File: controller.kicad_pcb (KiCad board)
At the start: 2 copper layers, 60 x 122 mm, 150 parts, among them J1 KYCON_KPJX-4S-S, J10 MicroFit_2x04, J11 Phoenix MPT, J12 MicroFit_2x04, J13 JST_B2B-XH, J14 Phoenix MPT, J16 MLX_1x03, J17 MLX_1x03, J2 MicroFit_2x02, J3 24V/5A OUT, J4 DB25 FEMALE, J5 Phoenix MPT, J6 Phoenix MPT, J7 MicroFit_2x04, J8 Phoenix MPT, J9 Phoenix MPT, K1 OJS-SH-124HMF, Q1 BC847, Q2 IRF9540SPBF, Q3 BC857, Q4 BC847, Q5 BC857, U1 MC78M12CDT-TR, U2 MAX5035BUSA, U3 LM358, U4 74HC245, U5 74HC245, U6 ACSL-6310, U7 ACSL-6310

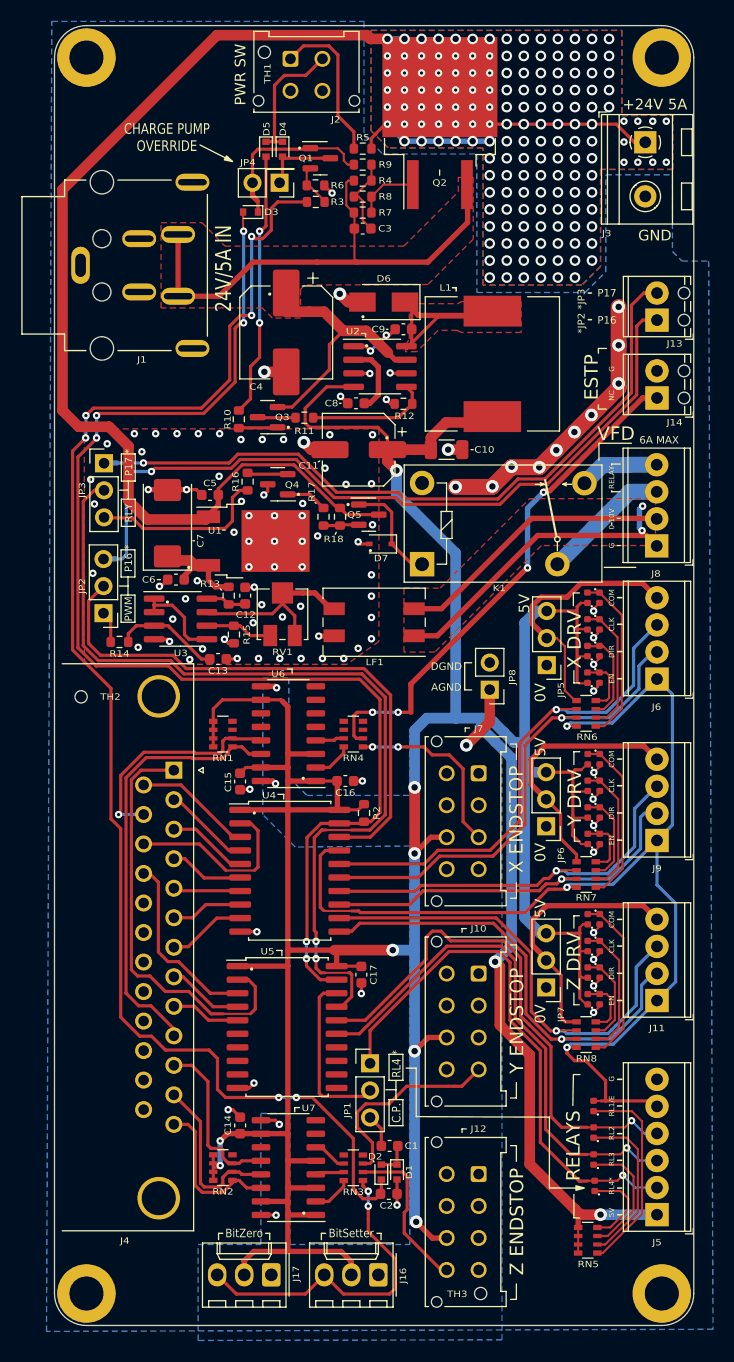
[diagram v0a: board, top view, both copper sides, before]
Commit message: Moved LPT left to protrude just over the PCB edge. Moved power connector inward to increase 24V/GND clearance.
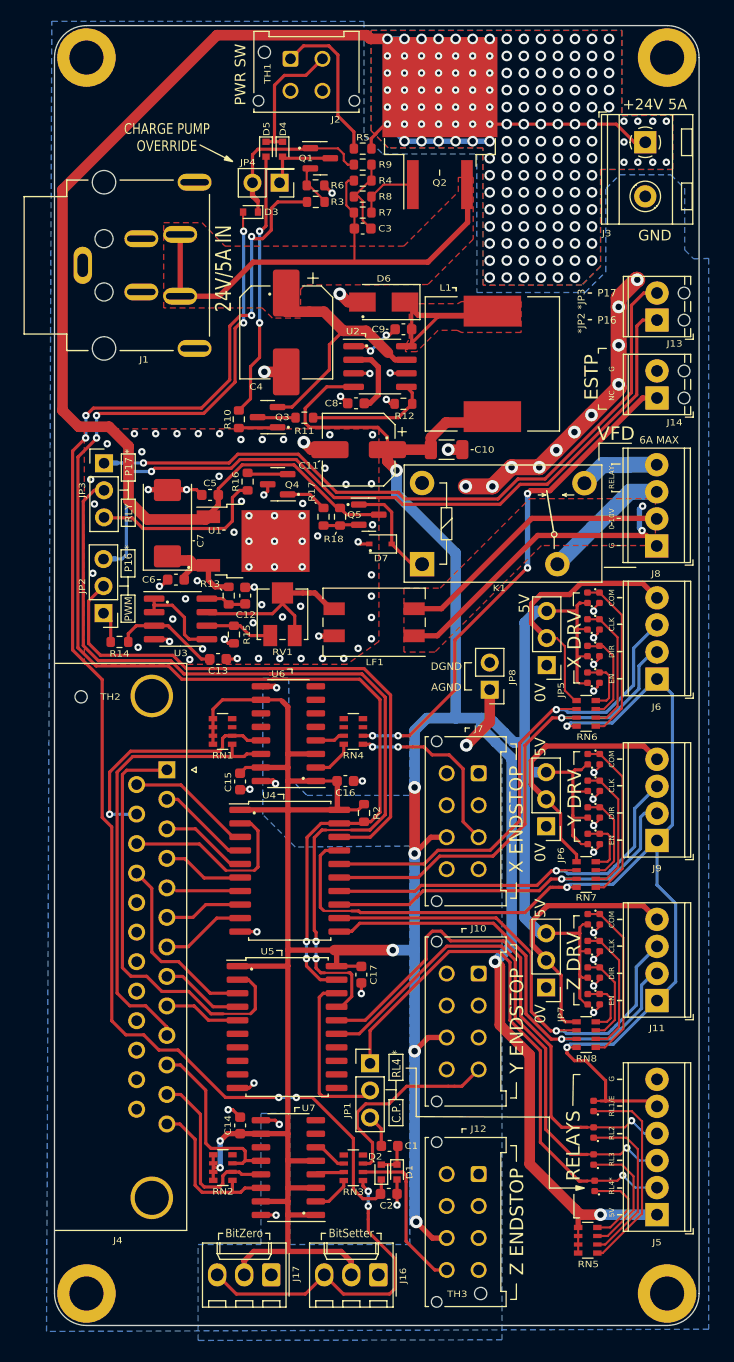
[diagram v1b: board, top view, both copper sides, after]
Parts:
- moved NT13 2.21 mm to (90.8, 112.0)
- moved J4 0.66 mm to (68.3, 115.2)
- moved H2 0.50 mm to (115.2, 48.4)
- moved H4 0.50 mm to (115.2, 164.4)
- moved NT20 0.44 mm to (104.8, 126.3)
- moved RN1 0.25 mm to (73.5, 111.7)
- moved RN4 0.24 mm to (85.8, 111.7)
- moved J1 0.20 mm to (69.5, 67.9)
- moved NT11 0.14 mm to (90.8, 153.6)
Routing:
- net /Connectors/EMERG_STOP_OUT: track 7.73 -> 3.75 mm
- net /Connectors/EMRG_STOP: track 40.2 -> 43.2 mm
- net GND: track 77.3 -> 79.7 mm, vias 101 -> 102
- net /LPT Interface/P10_OUT: track 41.1 -> 42.9 mm
- net /LPT Interface/P15_OUT: track 21.1 -> 22.8 mm
- net /LPT Interface/P11_OUT: track 16.0 -> 17.3 mm
- net /LPT Interface/P1_IN: track 39.8 -> 41.0 mm
- net /LPT Interface/P12_OUT: track 16.2 -> 17.3 mm
- net /LPT Interface/P2_IN: track 7.03 -> 8.10 mm
- net Net-(C2-Pad1): track 134.0 -> 133.0 mm
- net /LPT Interface/P17_IN: track 16.7 -> 17.6 mm
- net /LPT Interface/P8_IN: track 7.14 -> 7.81 mm
- net /LPT Interface/P16_IN: track 17.3 -> 17.9 mm
- net /LPT Interface/P14_IN: track 10.4 -> 11.1 mm
- net /LPT Interface/P9_IN: track 6.51 -> 7.18 mm
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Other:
- board size 60 x 122 mm -> 60.5 x 122 mm

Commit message: JLCPCB_V2.0_FROZEN
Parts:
- moved C10 2.78 mm to (97.3, 85.2), turned to 0 degrees
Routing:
- net GND: track 79.7 -> 85.2 mm, vias 102 -> 105
- net /Power/U2_FB: track 30.8 -> 33.4 mm
- net 24V_SAFE: track 133.9 -> 134.4 mm

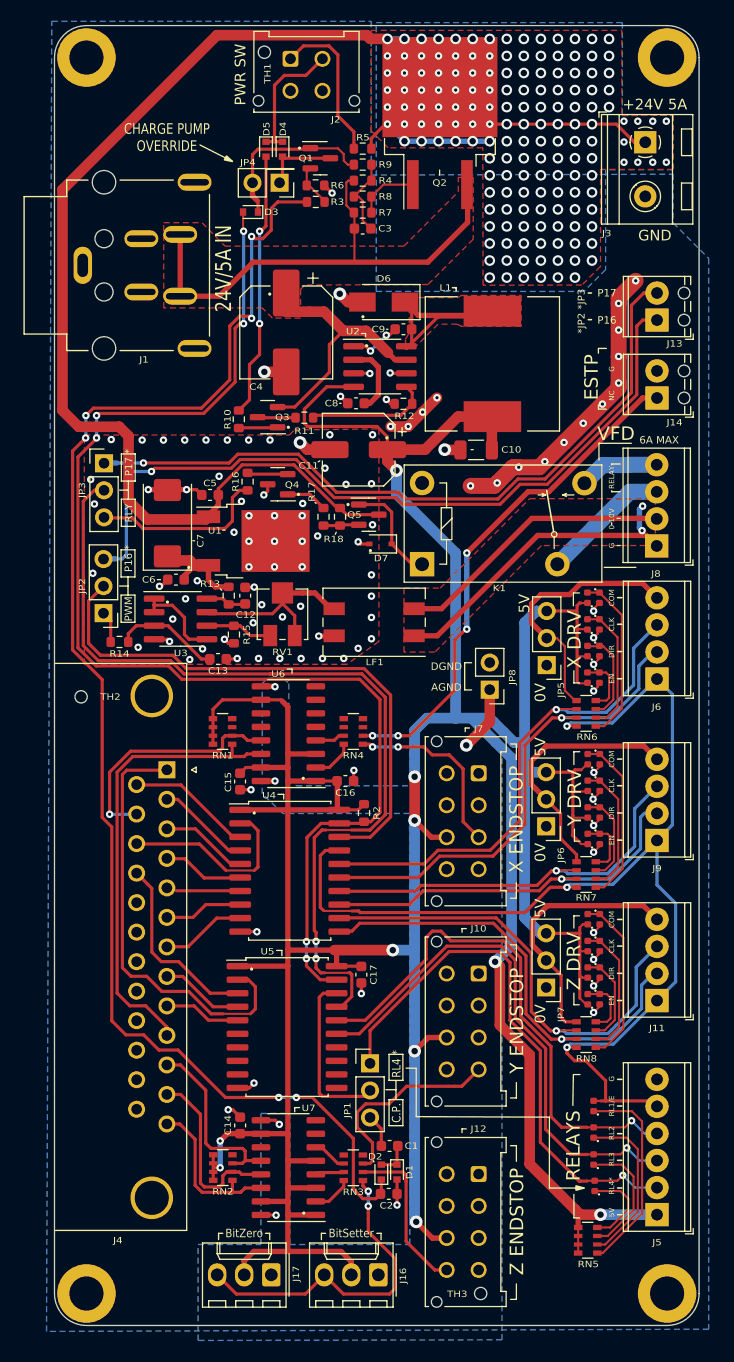
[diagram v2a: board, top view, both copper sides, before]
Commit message: V2.1 after errors found on physical V2.0 boards. sigh
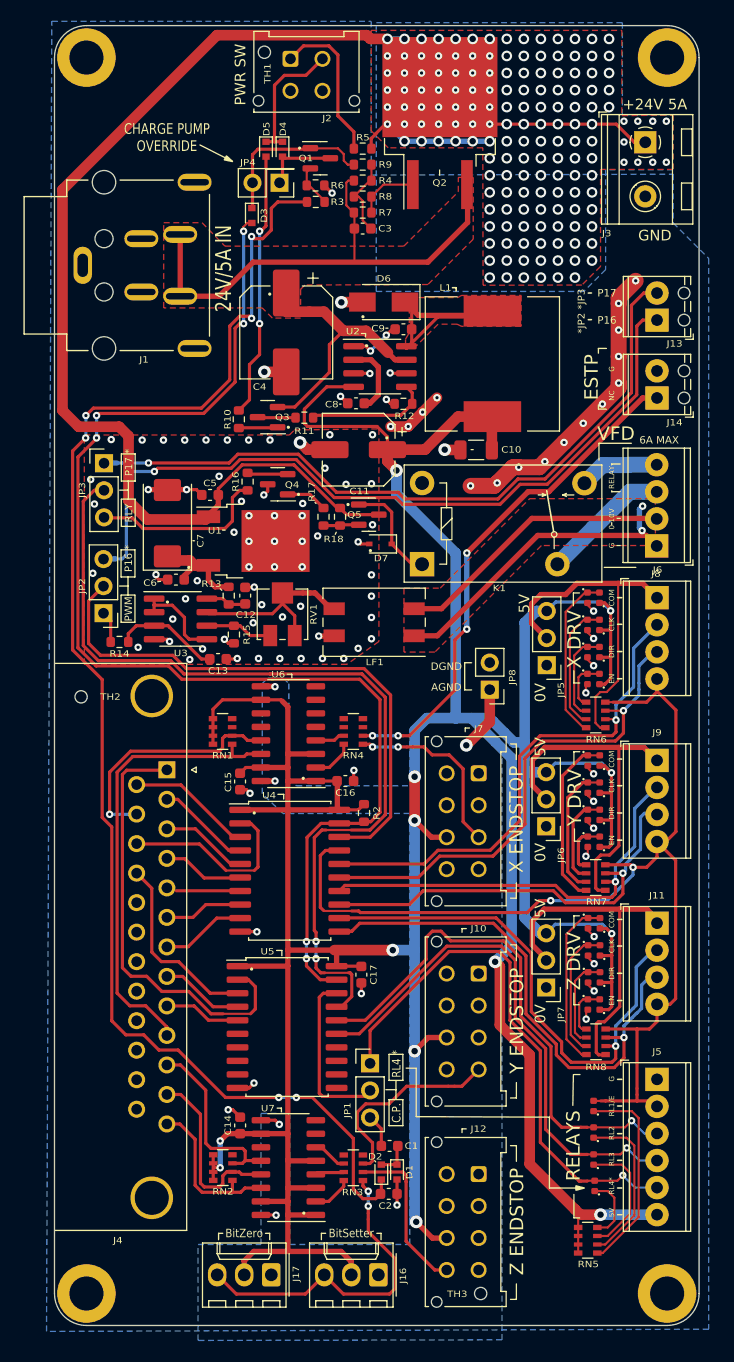
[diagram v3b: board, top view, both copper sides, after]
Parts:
- moved J5 12.7 mm to (114.3, 144.3), turned to -90 degrees
- moved D29 8.08 mm to (108.9, 137.3)
- moved D28 8.08 mm to (107.8, 137.3)
- moved D20 7.83 mm to (107.8, 122.0)
- moved D21 7.83 mm to (108.9, 122.0)
- moved D12 7.71 mm to (107.8, 106.7)
- moved D13 7.71 mm to (108.9, 106.7)
- moved J6 7.63 mm to (114.3, 99.1), turned to -90 degrees
- moved D18 7.58 mm to (107.8, 99.1)
- moved D19 7.58 mm to (108.9, 99.1)
- moved J9 7.51 mm to (114.3, 114.4), turned to -90 degrees
- moved D26 7.45 mm to (107.8, 114.4)
- moved D27 7.45 mm to (108.9, 114.4)
- moved J11 7.26 mm to (114.3, 129.6), turned to -90 degrees
- moved D35 7.22 mm to (109.0, 129.7)
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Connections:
- J11 pad 1: /Connectors/EN -> /Connectors/Z_COM
- J11 pad 2: /Connectors/ZDIR -> /Connectors/ZCLK
- J11 pad 3: /Connectors/ZCLK -> /Connectors/ZDIR
- J11 pad 4: /Connectors/Z_COM -> /Connectors/EN
- J5 pad 1: /Connectors/RELAY_5V -> GND
- J5 pad 2: /Connectors/RELAY4 -> /Connectors/RELAY1
- J5 pad 3: /Connectors/RELAY3 -> /Connectors/RELAY2
- J5 pad 4: /Connectors/RELAY2 -> /Connectors/RELAY3
- J5 pad 5: /Connectors/RELAY1 -> /Connectors/RELAY4
- J5 pad 6: GND -> /Connectors/RELAY_5V
- J6 pad 1: /Connectors/EN -> /Connectors/X_COM
- J6 pad 2: /Connectors/XDIR -> /Connectors/XCLK
- J6 pad 3: /Connectors/XCLK -> /Connectors/XDIR
- J6 pad 4: /Connectors/X_COM -> /Connectors/EN
- J9 pad 1: /Connectors/EN -> /Connectors/Y_COM
- J9 pad 2: /Connectors/YDIR -> /Connectors/YCLK
- J9 pad 3: /Connectors/YCLK -> /Connectors/YDIR
- J9 pad 4: /Connectors/Y_COM -> /Connectors/EN
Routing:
- net /Connectors/STP_5V: track 78.5 -> 91.7 mm, vias 0 -> 3
- net Net-(D28-Pad2): track 16.1 -> 5.03 mm
- net Net-(D12-Pad2): track 16.0 -> 4.96 mm
- net Net-(D20-Pad2): track 16.0 -> 5.08 mm
- net Net-(D26-Pad2): track 5.76 -> 16.4 mm
- net Net-(D34-Pad2): track 5.73 -> 16.1 mm
- net Net-(D18-Pad2): track 5.60 -> 15.7 mm
- net /Connectors/Y_COM: track 24.1 -> 32.5 mm
- net /Connectors/X_COM: track 24.4 -> 32.4 mm
- net /Connectors/Z_COM: track 24.4 -> 32.3 mm
- net /Connectors/ZDIR_IN: track 35.6 -> 42.5 mm
- net /Connectors/ZCLK_IN: track 35.3 -> 41.2 mm
- net /Connectors/YDIR_IN: track 28.0 -> 32.6 mm
- net /Connectors/RELAY1: track 11.2 -> 6.75 mm
- net /Connectors/XDIR_IN: track 38.0 -> 42.3 mm
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
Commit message: 'Final' tidy-up before trying physical boards production, yet again. Frankly, this is getting ridiculous. Never made so many mistakes on such a simple board. Getting too old? (51)
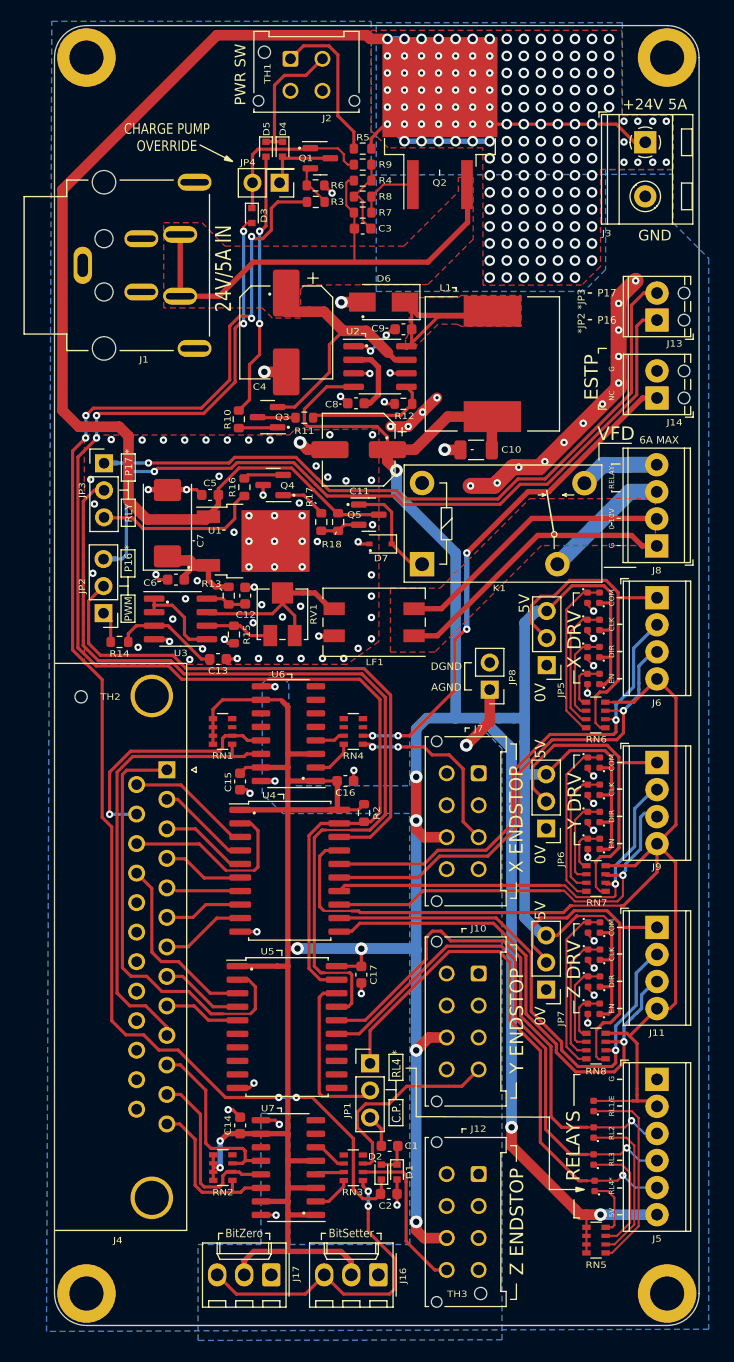
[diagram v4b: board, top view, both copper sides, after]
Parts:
- moved NT8 1.27 mm to (99.9, 112.5)
- moved NT27 1.11 mm to (100.2, 110.4), turned to 180 degrees
- moved RN5 0.78 mm to (108.6, 159.4)
- moved R16 0.61 mm to (75.6, 88.7)
- moved R17 0.53 mm to (82.8, 92.0)
- moved R18 0.52 mm to (84.4, 92.0)
- moved Q4 0.44 mm to (78.3, 88.5)
- moved D28 0.40 mm to (107.8, 137.7)
- moved D29 0.40 mm to (108.9, 137.7)
- moved D30 0.40 mm to (107.8, 135.1)
- moved D31 0.40 mm to (109.0, 135.1)
- moved D32 0.40 mm to (107.8, 132.6)
- moved D33 0.40 mm to (109.0, 132.6)
- moved D35 0.40 mm to (109.0, 130.0)
- moved RN8 0.40 mm to (108.6, 141.2)
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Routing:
- net /Connectors/STP_5V: track 91.7 -> 95.8 mm, vias 3 -> 0
- net /Connectors/VFD_AGND: track 29.6 -> 27.1 mm, vias 2 -> 0
- net /Connectors/RELAY_5V: track 60.4 -> 58.0 mm
- net +5V: track 235.5 -> 237.1 mm, vias 7 -> 8
- net /Connectors/EN: track 72.3 -> 73.6 mm, vias 2 -> 0
- net /Connectors/Y_COM: track 32.5 -> 31.4 mm
- net /LPT Interface/SPNDL_RELAY_IN: track 16.6 -> 15.6 mm
- net /Connectors/X_COM: track 32.4 -> 31.5 mm
- net /Connectors/ZDIR: track 4.78 -> 4.01 mm
- net Net-(Q5-Pad2): track 2.99 -> 3.76 mm
- net /Connectors/XDIR_IN: track 42.3 -> 41.5 mm
- net /Connectors/Z_COM: track 32.3 -> 31.5 mm
- net /Connectors/XCLK_IN: track 39.5 -> 38.7 mm
- net GND: track 85.5 -> 84.9 mm
- net /Connectors/ZCLK: track 6.75 -> 6.18 mm
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
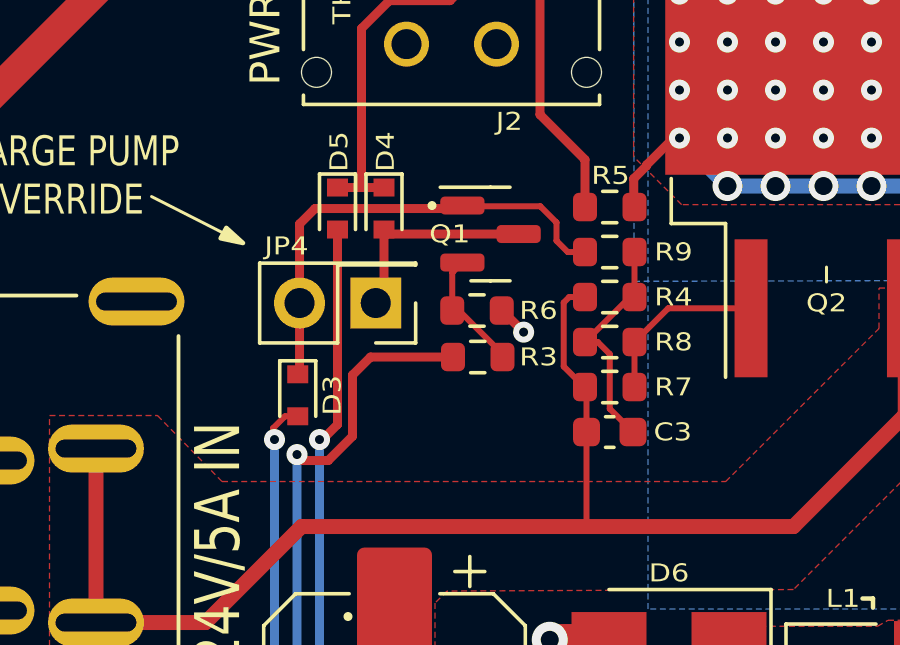
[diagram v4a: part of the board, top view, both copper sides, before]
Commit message: Correct Q1 pin muddle.
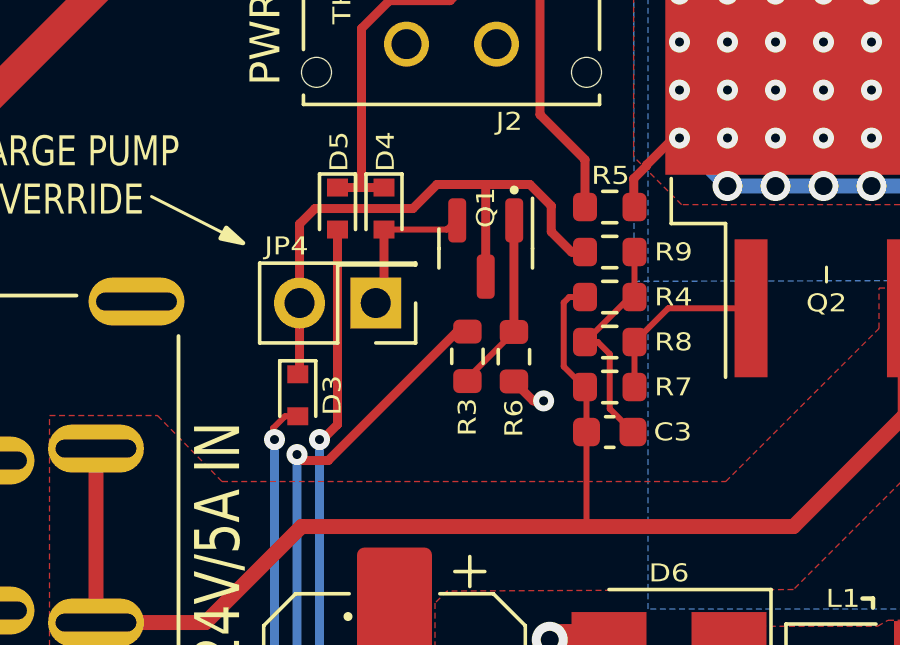
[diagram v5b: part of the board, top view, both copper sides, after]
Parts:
- moved R6 1.97 mm to (83.5, 61.9), turned to -90 degrees
- moved Q1 0.51 mm to (82.5, 58.3), turned to -90 degrees
- moved R3 0.34 mm to (81.9, 61.9), turned to -90 degrees
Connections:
- D3 pad 1: Net-(D3-Pad1) -> /Power/Q1_C
- D4 pad 2: Net-(D4-Pad2) -> /Power/Q1_E
- JP4 pad 1: Net-(D4-Pad2) -> /Power/Q1_E
- JP4 pad 2: Net-(D3-Pad1) -> /Power/Q1_C
- Q1 pad 1: Net-(D3-Pad1) -> /Power/Q1_B
- Q1 pad 2: Net-(Q1-Pad2) -> /Power/Q1_E
- Q1 pad 3: Net-(D4-Pad2) -> /Power/Q1_C
- R3 pad 2: Net-(Q1-Pad2) -> /Power/Q1_B
- R6 pad 1: Net-(Q1-Pad2) -> /Power/Q1_B
- R9 pad 2: Net-(D3-Pad1) -> /Power/Q1_C
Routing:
- net /Power/Q1_C: track 0.00 -> 19.5 mm
- net Net-(D3-Pad1): track 15.8 -> 0.00 mm
- net Net-(D4-Pad2): track 7.11 -> 0.00 mm
- net /Power/Q1_B: track 0.00 -> 6.00 mm
- net /Power/Q1_E: track 0.00 -> 5.13 mm
- net Net-(Q1-Pad2): track 4.12 -> 0.00 mm
